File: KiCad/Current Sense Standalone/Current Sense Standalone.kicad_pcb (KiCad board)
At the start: 2 copper layers, 62.3 x 24.3 mm, 11 parts, among them J1 PLUG INPUT BATTERY IN HERE (X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, J3 V+/- TEST Header PIN, J4 BAT +TERMINAL TEST HEADER PIN, J5 HEADER PIN FOR TEST, J6 to MCU GPIO PIN, J7 PLUG BATTERY OUTPUT HERE (XT6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, U1 INA139QPWRQ1

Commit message: Current Sense Update
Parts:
- C1: value 82pF -> 80pF
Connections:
- net Net-(J1-Pin_1) renamed /Batt+
- net Net-(J3-Pin_1) renamed /V-
- net Net-(J6-Pin_1) renamed /Vout
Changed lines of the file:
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@@
   )
   (net 0 "")
-  (net 1 "Net-(J6-Pin_1)")
+  (net 1 "/Vout")
   (net 2 "GND")
-  (net 3 "Net-(J3-Pin_1)")
-  (net 4 "Net-(J1-Pin_1)")
-  (net 5 "Net-(J7-Pin_1)")
-  (net 6 "unconnected-(U1-NC-Pad3)")
-  (net 7 "unconnected-(U1-NC-Pad5)")
-  (net 8 "unconnected-(U1-NC-Pad7)")
+  (net 3 "/V-")
+  (net 4 "Net-(J7-Pin_1)")
+  (net 5 "unconnected-(U1-NC-Pad3)")
+  (net 6 "unconnected-(U1-NC-Pad5)")
+  (net 7 "unconnected-(U1-NC-Pad7)")
+  (net 8 "/Batt+")
   (footprint "Mechatronic Footprints:AMASS_XT60-F_1x02_P7.20mm_Vertical" (layer "F.Cu")
     (at 168.674045 88.461822 -90)
@@
       (stroke (width 0.12) (type solid)) (layer "F.Fab"))
     (pad "1" thru_hole roundrect (at 0 0 270) (size 6 6) (drill 4.5) (layers "*.Cu" "*.Mask") (roundrect_rratio 0.25)
-      (net 5 "Net-(J7-Pin_1)") (pinfunction "Pin_1") (pintype "passive"))
+      (net 4 "Net-(J7-Pin_1)") (pinfunction "Pin_1") (pintype "passive"))
     (pad "2" thru_hole circle (at 7.2 0 270) (size 6 6) (drill 4.5) (layers "*.Cu" "*.Mask")
       (net 2 "GND") (pinfunction "Pin_2") (pintype "passive"))
@@
       (stroke (width 0.1) (type solid)) (layer "F.Fab"))
     (pad "1" smd roundrect (at -1.475 0 270) (size 1.15 1.8) (layers "F.Cu" "F.Paste" "F.Mask") (roundrect_rratio 0.2173913043)
-      (net 3 "Net-(J3-Pin_1)") (pintype "passive"))
+      (net 3 "/V-") (pintype "passive"))
     (pad "2" smd roundrect (at 1.475 0 270) (size 1.15 1.8) (layers "F.Cu" "F.Paste" "F.Mask") (roundrect_rratio 0.2173913043)
       (net 2 "GND") (pintype "passive"))
@@
       (stroke (width 0.1016) (type solid)) (layer "F.Fab"))
     (pad "1" smd rect (at -1.4 0 270) (size 1.6 1.8) (layers "F.Cu" "F.Paste" "F.Mask")
-      (net 1 "Net-(J6-Pin_1)") (pintype "passive"))
+      (net 1 "/Vout") (pintype "passive"))
     (pad "2" smd rect (at 1.4 0 270) (size 1.6 1.8) (layers "F.Cu" "F.Paste" "F.Mask")
       (net 2 "GND") (pintype "passive"))
@@
       (stroke (width 0.15) (type solid)) (layer "F.Fab"))
     (pad "1" smd rect (at -4.15 0 90) (size 2.7 6.2) (layers "F.Cu" "F.Paste" "F.Mask")
-      (net 5 "Net-(J7-Pin_1)") (pintype "passive"))
+      (net 4 "Net-(J7-Pin_1)") (pintype "passive"))
     (pad "2" smd rect (at 4.15 0 90) (size 2.7 6.2) (layers "F.Cu" "F.Paste" "F.Mask")
-      (net 4 "Net-(J1-Pin_1)") (pintype "passive"))
+      (net 8 "/Batt+") (pintype "passive"))
     (model "eec.models/Bourns_-_CSS2H-3920R-L300F.step"
       (offset (xyz 0 0 0))
@@
         (effects (font (size 1 1) (thickness 0.15)))
     )
-    (fp_text value "82pF" (at 3.114117 -0.115733 180) (layer "F.Fab")
+    (fp_text value "80pF" (at 3.114117 -0.115733 180) (layer "F.Fab")
         (effects (font (size 1 1) (thickness 0.15)))
     )
@@
       (stroke (width 0.1) (type solid)) (layer "F.Fab"))
     (pad "1" smd roundrect (at -1.475 0 270) (size 1.15 1.8) (layers "F.Cu" "F.Paste" "F.Mask") (roundrect_rratio 0.2173913043)
-      (net 1 "Net-(J6-Pin_1)") (pintype "passive"))
+      (net 1 "/Vout") (pintype "passive"))
     (pad "2" smd roundrect (at 1.475 0 270) (size 1.15 1.8) (layers "F.Cu" "F.Paste" "F.Mask") (roundrect_rratio 0.2173913043)
       (net 2 "GND") (pintype "passive"))
@@
       (stroke (width 0.1) (type solid)) (layer "F.Fab"))
     (pad "1" thru_hole rect (at 0 0 90) (size 1.7 1.7) (drill 1) (layers "*.Cu" "*.Mask")
-      (net 3 "Net-(J3-Pin_1)") (pinfunction "Pin_1") (pintype "passive"))
+      (net 3 "/V-") (pinfunction "Pin_1") (pintype "passive"))
     (pad "2" thru_hole oval (at 0 2.54 90) (size 1.7 1.7) (drill 1) (layers "*.Cu" "*.Mask"))
     (model "${KICAD6_3DMODEL_DIR}/Connector_PinHeader_2.54mm.3dshapes/PinHeader_1x02_P2.54mm_Vertical.wrl"
@@
       (stroke (width 0.1) (type solid)) (layer "F.Fab"))
     (pad "1" thru_hole rect (at 0 0 90) (size 1.7 1.7) (drill 1) (layers "*.Cu" "*.Mask")
-      (net 4 "Net-(J1-Pin_1)") (pinfunction "Pin_1") (pintype "passive"))
+      (net 8 "/Batt+") (pinfunction "Pin_1") (pintype "passive"))
     (pad "2" thru_hole oval (at 0 2.54 90) (size 1.7 1.7) (drill 1) (layers "*.Cu" "*.Mask"))
     (model "${KICAD6_3DMODEL_DIR}/Connector_PinHeader_2.54mm.3dshapes/PinHeader_1x02_P2.54mm_Vertical.wrl"
@@
       (stroke (width 0.0254) (type solid)) (layer "F.Fab"))
     (pad "1" smd rect (at -2.921 -0.974999) (size 1.4732 0.3556) (layers "F.Cu" "F.Paste" "F.Mask")
-      (net 5 "Net-(J7-Pin_1)") (pinfunction "VIN-") (pintype "input"))
+      (net 4 "Net-(J7-Pin_1)") (pinfunction "VIN-") (pintype "input"))
     (pad "2" smd rect (at -2.921 -0.325001) (size 1.4732 0.3556) (layers "F.Cu" "F.Paste" "F.Mask")
-      (net 4 "Net-(J1-Pin_1)") (pinfunction "VIN+") (pintype "input"))
+      (net 8 "/Batt+") (pinfunction "VIN+") (pintype "input"))
     (pad "3" smd rect (at -2.921 0.325001) (size 1.4732 0.3556) (layers "F.Cu" "F.Paste" "F.Mask")
-      (net 6 "unconnected-(U1-NC-Pad3)") (pinfunction "NC") (pintype "unspecified+no_connect"))
+      (net 5 "unconnected-(U1-NC-Pad3)") (pinfunction "NC") (pintype "unspecified+no_connect"))
     (pad "4" smd rect (at -2.921 0.974999) (size 1.4732 0.3556) (layers "F.Cu" "F.Paste" "F.Mask")
       (net 2 "GND") (pinfunction "GND") (pintype "power_in"))
     (pad "5" smd rect (at 2.921 0.974999) (size 1.4732 0.3556) (layers "F.Cu" "F.Paste" "F.Mask")
-      (net 7 "unconnected-(U1-NC-Pad5)") (pinfunction "NC") (pintype "unspecified+no_connect"))
+      (net 6 "unconnected-(U1-NC-Pad5)") (pinfunction "NC") (pintype "unspecified+no_connect"))
     (pad "6" smd rect (at 2.921 0.325001) (size 1.4732 0.3556) (layers "F.Cu" "F.Paste" "F.Mask")
-      (net 1 "Net-(J6-Pin_1)") (pinfunction "OUT") (pintype "output"))
+      (net 1 "/Vout") (pinfunction "OUT") (pintype "output"))
     (pad "7" smd rect (at 2.921 -0.325001) (size 1.4732 0.3556) (layers "F.Cu" "F.Paste" "F.Mask")
-      (net 8 "unconnected-(U1-NC-Pad7)") (pinfunction "NC") (pintype "unspecified+no_connect"))
+      (net 7 "unconnected-(U1-NC-Pad7)") (pinfunction "NC") (pintype "unspecified+no_connect"))
     (pad "8" smd rect (at 2.921 -0.974999) (size 1.4732 0.3556) (layers "F.Cu" "F.Paste" "F.Mask")
-      (net 3 "Net-(J3-Pin_1)") (pinfunction "V-") (pintype "power_in"))
+      (net 3 "/V-") (pinfunction "V-") (pintype "power_in"))
   )
   (footprint "Mechatronic Footprints:AMASS_XT60-M_1x02_P7.20mm_Vertical" (layer "F.Cu")
@@
       (stroke (width 0.12) (type solid)) (layer "F.Fab"))
     (pad "1" thru_hole roundrect (at 0 0 270) (size 6 6) (drill 4.5) (layers "*.Cu" "*.Mask") (roundrect_rratio 0.25)
-      (net 4 "Net-(J1-Pin_1)") (pinfunction "Pin_1") (pintype "passive"))
+      (net 8 "/Batt+") (pinfunction "Pin_1") (pintype "passive"))
     (pad "2" thru_hole circle (at 7.2 0 270) (size 6 6) (drill 4.5) (layers "*.Cu" "*.Mask")
       (net 2 "GND") (pinfunction "Pin_2") (pintype "passive"))
@@
       (stroke (width 0.1) (type solid)) (layer "F.Fab"))
     (pad "1" thru_hole rect (at 0 0 90) (size 1.7 1.7) (drill 1) (layers "*.Cu" "*.Mask")
-      (net 1 "Net-(J6-Pin_1)") (pinfunction "Pin_1") (pintype "passive"))
+      (net 1 "/Vout") (pinfunction "Pin_1") (pintype "passive"))
     (pad "2" thru_hole oval (at 0 2.54 90) (size 1.7 1.7) (drill 1) (layers "*.Cu" "*.Mask"))
     (model "${KICAD6_3DMODEL_DIR}/Connector_PinHeader_2.54mm.3dshapes/PinHeader_1x02_P2.54mm_Vertical.wrl"
@@
   (segment (start 144.78 88.9) (end 144.78 91.44) (width 0.25) (layer "B.Cu") (net 3))
   (segment (start 142.24 86.36) (end 144.78 88.9) (width 0.25) (layer "B.Cu") (net 3))
-  (segment (start 129.959273 91.948011) (end 132.64126 94.629998) (width 0.25) (layer "F.Cu") (net 4))
-  (segment (start 134.62 87.287284) (end 129.959273 91.948011) (width 0.25) (layer "F.Cu") (net 4))
-  (segment (start 132.64126 94.629998) (end 138.938 94.629998) (width 0.25) (layer "F.Cu") (net 4))
-  (segment (start 122.217974 91.948011) (end 129.959273 91.948011) (width 0.25) (layer "F.Cu") (net 4))
-  (segment (start 134.62 83.82) (end 134.62 87.287284) (width 0.25) (layer "F.Cu") (net 4))
-  (segment (start 118.980936 88.710973) (end 122.217974 91.948011) (width 0.25) (layer "F.Cu") (net 4))
-  (segment (start 156.887856 100.248011) (end 168.674045 88.461822) (width 0.25) (layer "F.Cu") (net 5))
-  (segment (start 144.456178 88.461822) (end 138.938 93.98) (width 0.25) (layer "F.Cu") (net 5))
-  (segment (start 129.959273 100.248011) (end 156.887856 100.248011) (width 0.25) (layer "F.Cu") (net 5))
-  (segment (start 168.674045 88.461822) (end 144.456178 88.461822) (width 0.25) (layer "F.Cu") (net 5))
+  (segment (start 156.887856 100.248011) (end 168.674045 88.461822) (width 0.25) (layer "F.Cu") (net 4))
+  (segment (start 144.456178 88.461822) (end 138.938 93.98) (width 0.25) (layer "F.Cu") (net 4))
+  (segment (start 129.959273 100.248011) (end 156.887856 100.248011) (width 0.25) (layer "F.Cu") (net 4))
+  (segment (start 168.674045 88.461822) (end 144.456178 88.461822) (width 0.25) (layer "F.Cu") (net 4))
+  (segment (start 129.959273 91.948011) (end 132.64126 94.629998) (width 0.25) (layer "F.Cu") (net 8))
+  (segment (start 134.62 87.287284) (end 129.959273 91.948011) (width 0.25) (layer "F.Cu") (net 8))
+  (segment (start 132.64126 94.629998) (end 138.938 94.629998) (width 0.25) (layer "F.Cu") (net 8))
+  (segment (start 122.217974 91.948011) (end 129.959273 91.948011) (width 0.25) (layer "F.Cu") (net 8))
+  (segment (start 134.62 83.82) (end 134.62 87.287284) (width 0.25) (layer "F.Cu") (net 8))
+  (segment (start 118.980936 88.710973) (end 122.217974 91.948011) (width 0.25) (layer "F.Cu") (net 8))
   (zone (net 2) (net_name "GND") (layers "F&B.Cu") (hatch edge 0.5)
     (connect_pads yes (clearance 0.5))

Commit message: Current Sense Update
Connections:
- net Net-(J7-Pin_1) renamed /Batt-
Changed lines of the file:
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@@
   (net 2 "GND")
   (net 3 "/V-")
-  (net 4 "Net-(J7-Pin_1)")
-  (net 5 "unconnected-(U1-NC-Pad3)")
-  (net 6 "unconnected-(U1-NC-Pad5)")
-  (net 7 "unconnected-(U1-NC-Pad7)")
-  (net 8 "/Batt+")
+  (net 4 "unconnected-(U1-NC-Pad3)")
+  (net 5 "unconnected-(U1-NC-Pad5)")
+  (net 6 "unconnected-(U1-NC-Pad7)")
+  (net 7 "/Batt+")
+  (net 8 "/Batt-")
   (footprint "Mechatronic Footprints:AMASS_XT60-F_1x02_P7.20mm_Vertical" (layer "F.Cu")
     (at 168.674045 88.461822 -90)
@@
       (stroke (width 0.12) (type solid)) (layer "F.Fab"))
     (pad "1" thru_hole roundrect (at 0 0 270) (size 6 6) (drill 4.5) (layers "*.Cu" "*.Mask") (roundrect_rratio 0.25)
-      (net 4 "Net-(J7-Pin_1)") (pinfunction "Pin_1") (pintype "passive"))
+      (net 8 "/Batt-") (pinfunction "Pin_1") (pintype "passive"))
     (pad "2" thru_hole circle (at 7.2 0 270) (size 6 6) (drill 4.5) (layers "*.Cu" "*.Mask")
       (net 2 "GND") (pinfunction "Pin_2") (pintype "passive"))
@@
       (stroke (width 0.15) (type solid)) (layer "F.Fab"))
     (pad "1" smd rect (at -4.15 0 90) (size 2.7 6.2) (layers "F.Cu" "F.Paste" "F.Mask")
-      (net 4 "Net-(J7-Pin_1)") (pintype "passive"))
+      (net 8 "/Batt-") (pintype "passive"))
     (pad "2" smd rect (at 4.15 0 90) (size 2.7 6.2) (layers "F.Cu" "F.Paste" "F.Mask")
-      (net 8 "/Batt+") (pintype "passive"))
+      (net 7 "/Batt+") (pintype "passive"))
     (model "eec.models/Bourns_-_CSS2H-3920R-L300F.step"
       (offset (xyz 0 0 0))
@@
       (stroke (width 0.1) (type solid)) (layer "F.Fab"))
     (pad "1" thru_hole rect (at 0 0 90) (size 1.7 1.7) (drill 1) (layers "*.Cu" "*.Mask")
-      (net 8 "/Batt+") (pinfunction "Pin_1") (pintype "passive"))
+      (net 7 "/Batt+") (pinfunction "Pin_1") (pintype "passive"))
     (pad "2" thru_hole oval (at 0 2.54 90) (size 1.7 1.7) (drill 1) (layers "*.Cu" "*.Mask"))
     (model "${KICAD6_3DMODEL_DIR}/Connector_PinHeader_2.54mm.3dshapes/PinHeader_1x02_P2.54mm_Vertical.wrl"
@@
       (stroke (width 0.0254) (type solid)) (layer "F.Fab"))
     (pad "1" smd rect (at -2.921 -0.974999) (size 1.4732 0.3556) (layers "F.Cu" "F.Paste" "F.Mask")
-      (net 4 "Net-(J7-Pin_1)") (pinfunction "VIN-") (pintype "input"))
+      (net 8 "/Batt-") (pinfunction "VIN-") (pintype "input"))
     (pad "2" smd rect (at -2.921 -0.325001) (size 1.4732 0.3556) (layers "F.Cu" "F.Paste" "F.Mask")
-      (net 8 "/Batt+") (pinfunction "VIN+") (pintype "input"))
+      (net 7 "/Batt+") (pinfunction "VIN+") (pintype "input"))
     (pad "3" smd rect (at -2.921 0.325001) (size 1.4732 0.3556) (layers "F.Cu" "F.Paste" "F.Mask")
-      (net 5 "unconnected-(U1-NC-Pad3)") (pinfunction "NC") (pintype "unspecified+no_connect"))
+      (net 4 "unconnected-(U1-NC-Pad3)") (pinfunction "NC") (pintype "unspecified+no_connect"))
     (pad "4" smd rect (at -2.921 0.974999) (size 1.4732 0.3556) (layers "F.Cu" "F.Paste" "F.Mask")
       (net 2 "GND") (pinfunction "GND") (pintype "power_in"))
     (pad "5" smd rect (at 2.921 0.974999) (size 1.4732 0.3556) (layers "F.Cu" "F.Paste" "F.Mask")
-      (net 6 "unconnected-(U1-NC-Pad5)") (pinfunction "NC") (pintype "unspecified+no_connect"))
+      (net 5 "unconnected-(U1-NC-Pad5)") (pinfunction "NC") (pintype "unspecified+no_connect"))
     (pad "6" smd rect (at 2.921 0.325001) (size 1.4732 0.3556) (layers "F.Cu" "F.Paste" "F.Mask")
       (net 1 "/Vout") (pinfunction "OUT") (pintype "output"))
     (pad "7" smd rect (at 2.921 -0.325001) (size 1.4732 0.3556) (layers "F.Cu" "F.Paste" "F.Mask")
-      (net 7 "unconnected-(U1-NC-Pad7)") (pinfunction "NC") (pintype "unspecified+no_connect"))
+      (net 6 "unconnected-(U1-NC-Pad7)") (pinfunction "NC") (pintype "unspecified+no_connect"))
     (pad "8" smd rect (at 2.921 -0.974999) (size 1.4732 0.3556) (layers "F.Cu" "F.Paste" "F.Mask")
       (net 3 "/V-") (pinfunction "V-") (pintype "power_in"))
@@
       (stroke (width 0.12) (type solid)) (layer "F.Fab"))
     (pad "1" thru_hole roundrect (at 0 0 270) (size 6 6) (drill 4.5) (layers "*.Cu" "*.Mask") (roundrect_rratio 0.25)
-      (net 8 "/Batt+") (pinfunction "Pin_1") (pintype "passive"))
+      (net 7 "/Batt+") (pinfunction "Pin_1") (pintype "passive"))
     (pad "2" thru_hole circle (at 7.2 0 270) (size 6 6) (drill 4.5) (layers "*.Cu" "*.Mask")
       (net 2 "GND") (pinfunction "Pin_2") (pintype "passive"))
@@
   (segment (start 144.78 88.9) (end 144.78 91.44) (width 0.25) (layer "B.Cu") (net 3))
   (segment (start 142.24 86.36) (end 144.78 88.9) (width 0.25) (layer "B.Cu") (net 3))
-  (segment (start 156.887856 100.248011) (end 168.674045 88.461822) (width 0.25) (layer "F.Cu") (net 4))
-  (segment (start 144.456178 88.461822) (end 138.938 93.98) (width 0.25) (layer "F.Cu") (net 4))
-  (segment (start 129.959273 100.248011) (end 156.887856 100.248011) (width 0.25) (layer "F.Cu") (net 4))
-  (segment (start 168.674045 88.461822) (end 144.456178 88.461822) (width 0.25) (layer "F.Cu") (net 4))
-  (segment (start 129.959273 91.948011) (end 132.64126 94.629998) (width 0.25) (layer "F.Cu") (net 8))
-  (segment (start 134.62 87.287284) (end 129.959273 91.948011) (width 0.25) (layer "F.Cu") (net 8))
-  (segment (start 132.64126 94.629998) (end 138.938 94.629998) (width 0.25) (layer "F.Cu") (net 8))
-  (segment (start 122.217974 91.948011) (end 129.959273 91.948011) (width 0.25) (layer "F.Cu") (net 8))
-  (segment (start 134.62 83.82) (end 134.62 87.287284) (width 0.25) (layer "F.Cu") (net 8))
-  (segment (start 118.980936 88.710973) (end 122.217974 91.948011) (width 0.25) (layer "F.Cu") (net 8))
+  (segment (start 129.959273 91.948011) (end 132.64126 94.629998) (width 0.25) (layer "F.Cu") (net 7))
+  (segment (start 134.62 87.287284) (end 129.959273 91.948011) (width 0.25) (layer "F.Cu") (net 7))
+  (segment (start 132.64126 94.629998) (end 138.938 94.629998) (width 0.25) (layer "F.Cu") (net 7))
+  (segment (start 122.217974 91.948011) (end 129.959273 91.948011) (width 0.25) (layer "F.Cu") (net 7))
+  (segment (start 134.62 83.82) (end 134.62 87.287284) (width 0.25) (layer "F.Cu") (net 7))
+  (segment (start 118.980936 88.710973) (end 122.217974 91.948011) (width 0.25) (layer "F.Cu") (net 7))
+  (segment (start 156.887856 100.248011) (end 168.674045 88.461822) (width 0.25) (layer "F.Cu") (net 8))
+  (segment (start 144.456178 88.461822) (end 138.938 93.98) (width 0.25) (layer "F.Cu") (net 8))
+  (segment (start 129.959273 100.248011) (end 156.887856 100.248011) (width 0.25) (layer "F.Cu") (net 8))
+  (segment (start 168.674045 88.461822) (end 144.456178 88.461822) (width 0.25) (layer "F.Cu") (net 8))
   (zone (net 2) (net_name "GND") (layers "F&B.Cu") (hatch edge 0.5)
     (connect_pads yes (clearance 0.5))

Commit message: Updated Current Sense Standalone
new footprint for R_SENSE and fixed header pins
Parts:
- Rs1: footprint Res_Bourns_CSS2H-3920R-L300F:Bourns-CSS2H-3920R-L300F-MFG -> Mechatronic Footprints:CSS2H-5930R
- moved J7 9.33 mm to (168.7, 97.8), turned to 90 degrees
- moved J1 9.08 mm to (119.0, 97.8), turned to 90 degrees
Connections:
- J1 pad 1: /Batt+ -> GND
- J1 pad 2: GND -> /Batt+
- J3 pad 2: (no net) -> GND
- J4 pad 2: (no net) -> GND
- J6 pad 2: (no net) -> GND
- J7 pad 1: /Batt- -> GND
- J7 pad 2: GND -> /Batt-
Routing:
- net GND: track 0.00 -> 28.7 mm
- net /Batt+: track 32.5 -> 34.1 mm

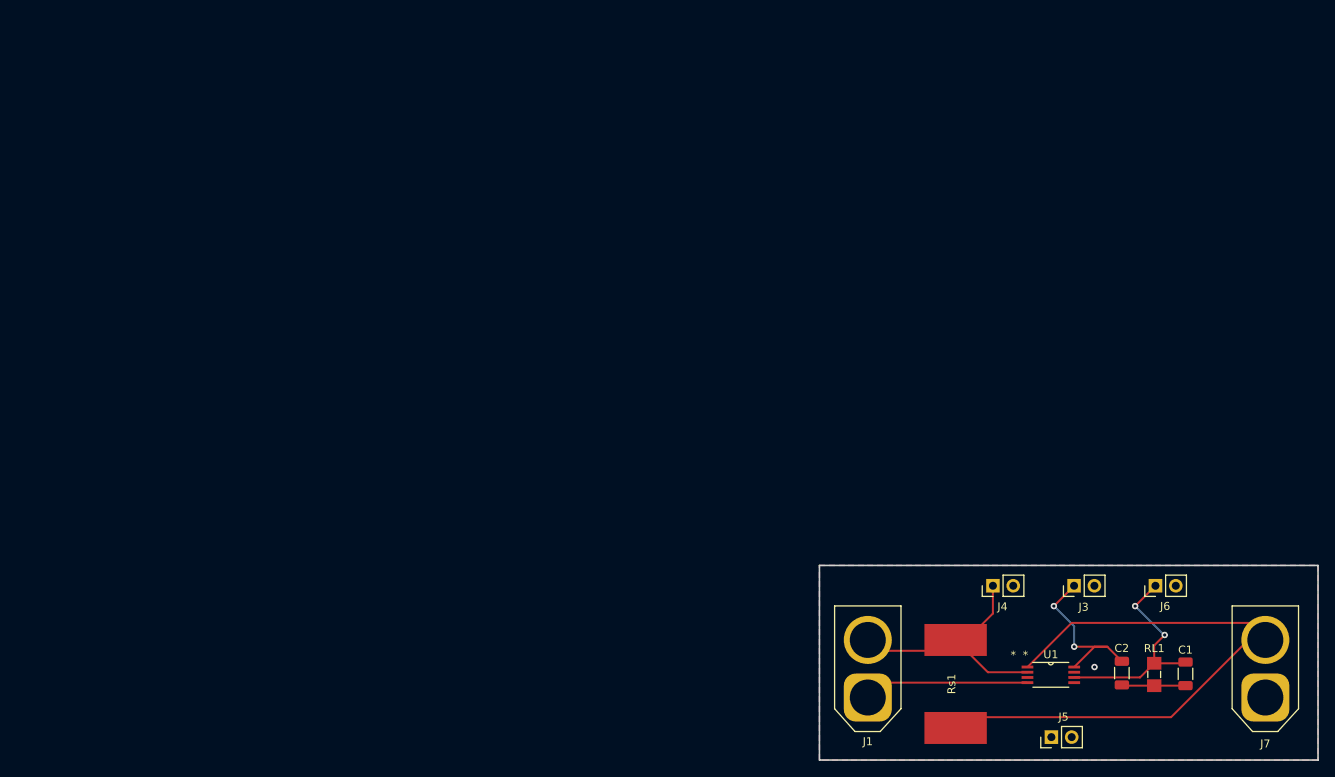
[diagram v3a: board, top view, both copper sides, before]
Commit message: Mill Current Sense PCB
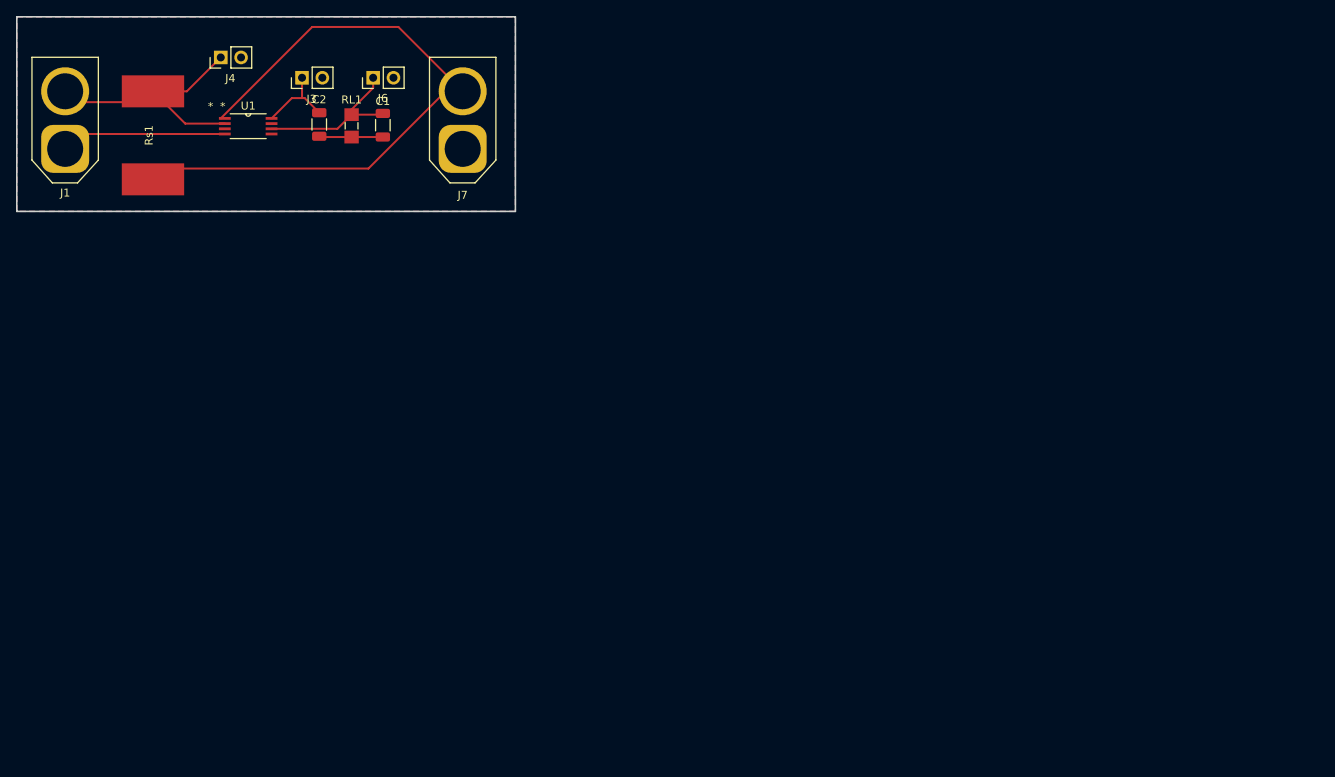
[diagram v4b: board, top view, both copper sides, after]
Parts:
- removed J5: HEADER PIN FOR TEST, Connector_PinHeader_2.54mm:PinHeader_1x02_P2.54mm_Vertical
- moved C1 121.5 mm to (58.4, 26.2)
- moved C2 121.5 mm to (50.4, 26.2)
- moved J7 121.5 mm to (68.3, 29.2)
- moved RL1 121.5 mm to (54.5, 26.3)
- moved U1 121.5 mm to (41.5, 26.4)
- moved J1 121.5 mm to (18.7, 29.2)
- moved Rs1 121.5 mm to (29.6, 27.5)
- moved J4 117.0 mm to (38.1, 17.8)
- moved J6 116.6 mm to (57.1, 20.3)
- moved J3 115.5 mm to (48.3, 20.3)
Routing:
- net /V-: track 21.6 -> 10.3 mm, vias 2 -> 0
- net /Vout: track 27.6 -> 20.4 mm, vias 2 -> 0
- net /Batt-: track 75.6 -> 81.0 mm
- net /Batt+: track 34.1 -> 34.9 mm
- net GND: vias 1 -> 0
